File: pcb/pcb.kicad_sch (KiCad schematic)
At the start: 65 parts, among them J1 USB_C_Receptacle_USB2.0, SW1 SW_Push, SW2 SW_Push, U1 SRV05-4, U2 XC6206P332MR, U3 DRV5056A3xDBZxQ1, U4 DRV5056A3xDBZxQ1, U5 DRV5056A3xDBZxQ1, U6 74AHCT1G125, U7 74AHCT1G125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

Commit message: fix: use grounded 3.5mm mounting holes on pcb didn't realise that the pads are used for grounding... definitely worth adding them in.
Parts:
- H1, H2, H3, H4: footprint MountingHole:MountingHole_4mm -> MountingHole:MountingHole_3.5mm_Pad
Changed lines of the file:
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@@
       (effects (font (size 1.27 1.27)) (justify left))
     )
-    (property "Footprint" "MountingHole:MountingHole_4mm" (at 198.12 172.72 0)
+    (property "Footprint" "MountingHole:MountingHole_3.5mm_Pad" (at 198.12 172.72 0)
       (effects (font (size 1.27 1.27)) hide)
     )
@@
       (effects (font (size 1.27 1.27)) (justify left))
     )
-    (property "Footprint" "MountingHole:MountingHole_4mm" (at 218.44 172.72 0)
+    (property "Footprint" "MountingHole:MountingHole_3.5mm_Pad" (at 218.44 172.72 0)
       (effects (font (size 1.27 1.27)) hide)
     )
@@
       (effects (font (size 1.27 1.27)) (justify left))
     )
-    (property "Footprint" "MountingHole:MountingHole_4mm" (at 177.8 172.72 0)
+    (property "Footprint" "MountingHole:MountingHole_3.5mm_Pad" (at 177.8 172.72 0)
       (effects (font (size 1.27 1.27)) hide)
     )
@@
       (effects (font (size 1.27 1.27)) (justify left))
     )
-    (property "Footprint" "MountingHole:MountingHole_4mm" (at 238.76 172.72 0)
-      (effects (font (size 1.27 1.27)) hide)
-    )
+    (property "Footprint" "MountingHole:MountingHole_3.5mm_Pad" (at 238.76 172.72 0)
+      (effects (font (size 1.27 1.27)) hide)
+    )

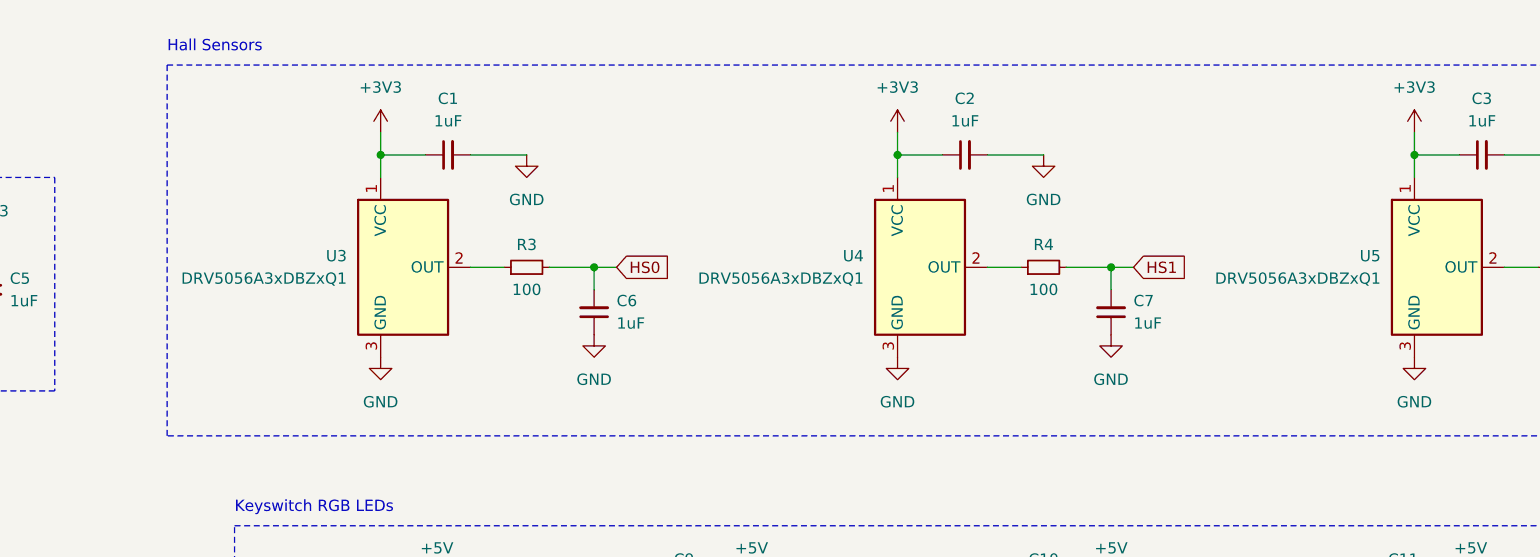
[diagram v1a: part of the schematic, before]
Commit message: fix: use DRV5056A4
not in stock at JLC, but it's the better option as it can detect the full range while being better than any bipolar options.
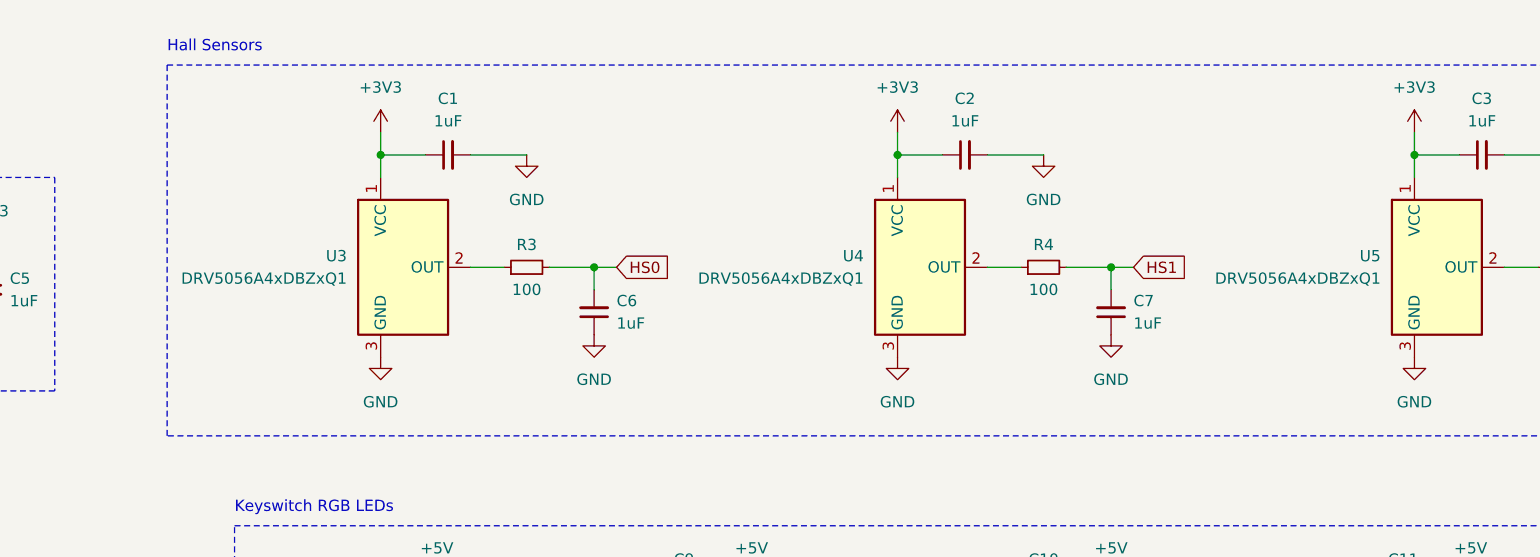
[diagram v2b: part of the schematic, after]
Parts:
- U3, U4, U5: value DRV5056A3xDBZxQ1 -> DRV5056A4xDBZxQ1; footprint Custom:KS-20-1U-DRV5056 -> Package_TO_SOT_SMD:SOT-23; symbol Harukapad:DRV5056A3xDBZxQ1 -> Custom:DRV5056A4xDBZxQ1; LCSC C2152965 -> C2152902
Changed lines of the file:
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@@
     )
   )
-  (symbol (lib_id "Harukapad:DRV5056A3xDBZxQ1") (at 186.69 44.45 0) (unit 1)
+  (symbol (lib_id "Custom:DRV5056A4xDBZxQ1") (at 186.69 44.45 0) (unit 1)
     (in_bom yes) (on_board yes) (dnp no) (fields_autoplaced)
     (property "Reference" "U3" (at 180.34 43.18 0)
       (effects (font (size 1.27 1.27)) (justify right))
     )
-    (property "Value" "DRV5056A3xDBZxQ1" (at 180.34 45.72 0)
+    (property "Value" "DRV5056A4xDBZxQ1" (at 180.34 45.72 0)
       (effects (font (size 1.27 1.27)) (justify right))
     )
-    (property "Footprint" "Custom:KS-20-1U-DRV5056" (at 186.69 44.45 0)
+    (property "Footprint" "Package_TO_SOT_SMD:SOT-23" (at 186.69 44.45 0)
       (effects (font (size 1.27 1.27)) hide)
     )
@@
       (effects (font (size 1.27 1.27)) hide)
     )
-    (property "LCSC" "C2152965" (at 186.69 44.45 0)
+    (property "LCSC" "C2152902" (at 186.69 44.45 0)
       (effects (font (size 1.27 1.27)) hide)
     )
@@
     )
   )
-  (symbol (lib_id "Harukapad:DRV5056A3xDBZxQ1") (at 303.53 44.45 0) (unit 1)
+  (symbol (lib_id "Custom:DRV5056A4xDBZxQ1") (at 303.53 44.45 0) (unit 1)
     (in_bom yes) (on_board yes) (dnp no) (fields_autoplaced)
     (property "Reference" "U5" (at 297.18 43.18 0)
       (effects (font (size 1.27 1.27)) (justify right))
     )
-    (property "Value" "DRV5056A3xDBZxQ1" (at 297.18 45.72 0)
+    (property "Value" "DRV5056A4xDBZxQ1" (at 297.18 45.72 0)
       (effects (font (size 1.27 1.27)) (justify right))
     )
-    (property "Footprint" "Custom:KS-20-1U-DRV5056" (at 303.53 44.45 0)
+    (property "Footprint" "Package_TO_SOT_SMD:SOT-23" (at 303.53 44.45 0)
       (effects (font (size 1.27 1.27)) hide)
     )
@@
       (effects (font (size 1.27 1.27)) hide)
     )
-    (property "LCSC" "C2152965" (at 303.53 44.45 0)
+    (property "LCSC" "C2152902" (at 303.53 44.45 0)
       (effects (font (size 1.27 1.27)) hide)
     )
@@
     )
   )
-  (symbol (lib_id "Harukapad:DRV5056A3xDBZxQ1") (at 245.11 44.45 0) (unit 1)
+  (symbol (lib_id "Custom:DRV5056A4xDBZxQ1") (at 245.11 44.45 0) (unit 1)
     (in_bom yes) (on_board yes) (dnp no) (fields_autoplaced)
     (property "Reference" "U4" (at 238.76 43.18 0)
       (effects (font (size 1.27 1.27)) (justify right))
     )
-    (property "Value" "DRV5056A3xDBZxQ1" (at 238.76 45.72 0)
+    (property "Value" "DRV5056A4xDBZxQ1" (at 238.76 45.72 0)
       (effects (font (size 1.27 1.27)) (justify right))
     )
-    (property "Footprint" "Custom:KS-20-1U-DRV5056" (at 245.11 44.45 0)
+    (property "Footprint" "Package_TO_SOT_SMD:SOT-23" (at 245.11 44.45 0)
       (effects (font (size 1.27 1.27)) hide)
     )
@@
       (effects (font (size 1.27 1.27)) hide)
     )
-    (property "LCSC" "C2152965" (at 245.11 44.45 0)
-      (effects (font (size 1.27 1.27)) hide)
-    )
+    (property "LCSC" "C2152902" (at 245.11 44.45 0)
+      (effects (font (size 1.27 1.27)) hide)
+    )
